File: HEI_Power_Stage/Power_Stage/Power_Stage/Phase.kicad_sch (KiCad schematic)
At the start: 41 parts, among them IC1 ACS730KLCTR-65ABT, IC5 AHV85111KNHTR, IC6 AHV85111KNHTR, Q1 EPC2304ENGRT, Q2 EPC2304ENGRT

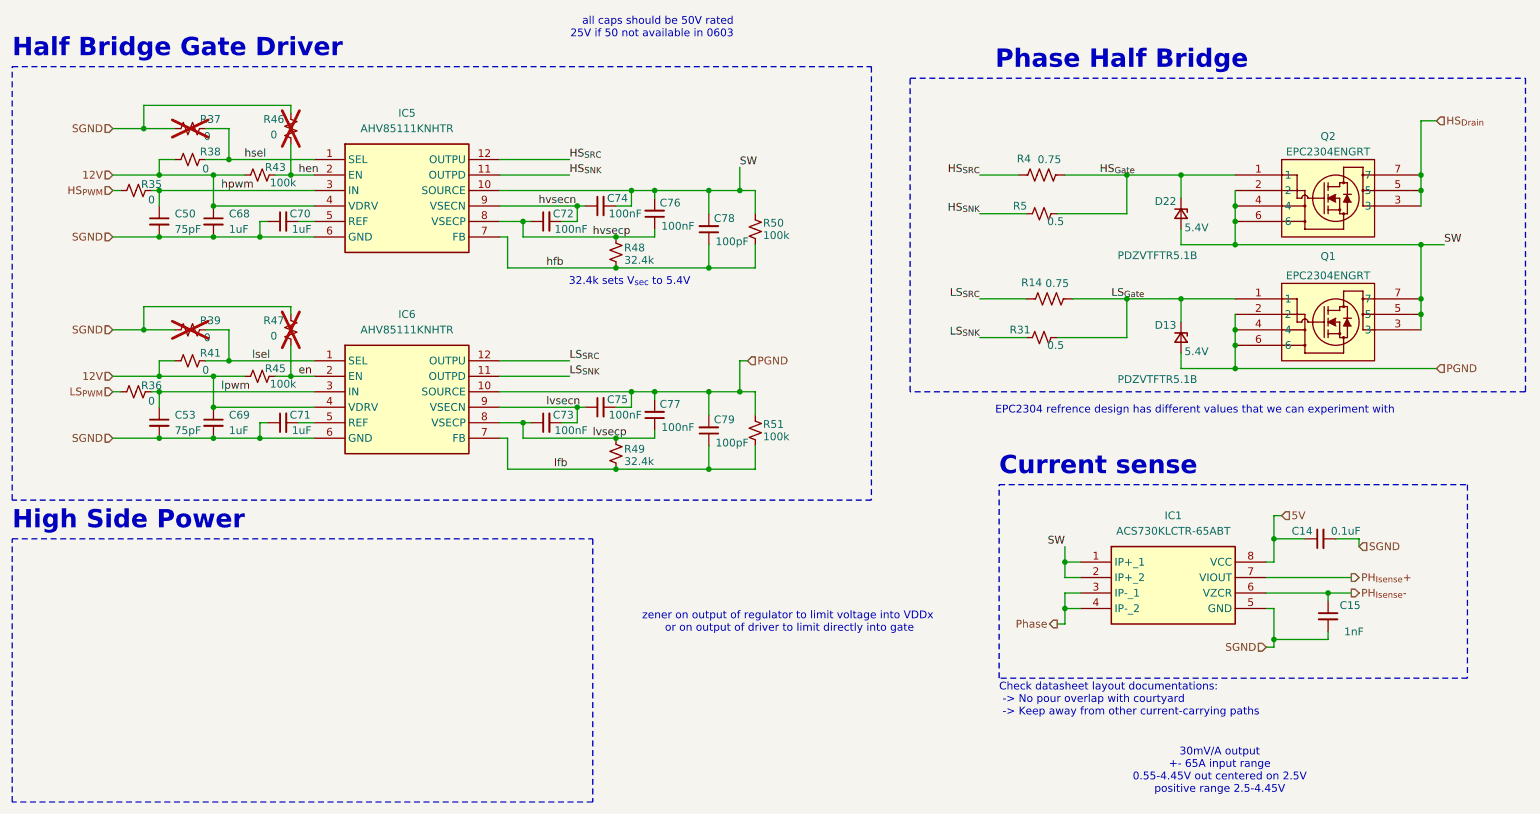
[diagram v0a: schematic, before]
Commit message: done
silkscreen done and bom done in digikey
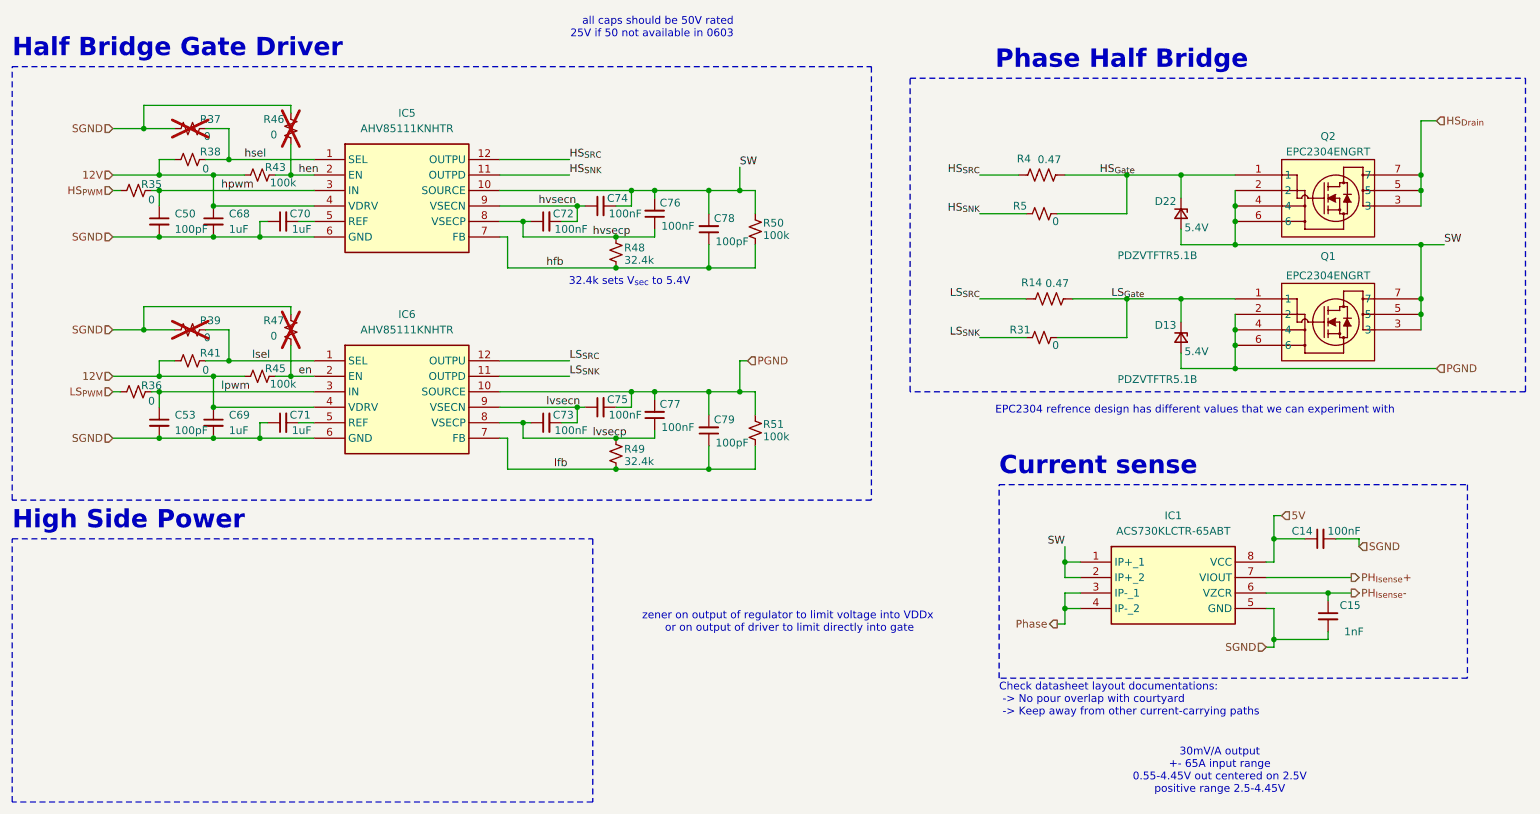
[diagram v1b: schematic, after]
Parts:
- C14: value 0.1uF -> 100nF
- C50, C53: value 75pF -> 100pF
- R14, R4: value 0.75 -> 0.47
- R31, R5: value 0.5 -> 0
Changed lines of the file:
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@@
 			)
 		)
-		(property "Value" "0.75"
+		(property "Value" "0.47"
 			(at 191.77 74.93 90)
 			(effects
@@
 			)
 		)
-		(property "Value" "0.1uF"
+		(property "Value" "100nF"
 			(at 241.554 115.57 90)
 			(effects
@@
 			)
 		)
-		(property "Value" "0.5"
+		(property "Value" "0"
 			(at 191.516 85.09 90)
 			(effects
@@
 			)
 		)
-		(property "Value" "0.75"
+		(property "Value" "0.47"
 			(at 190.5 54.61 90)
 			(effects
@@
 			)
 		)
-		(property "Value" "75pF"
+		(property "Value" "100pF"
 			(at 46.99 66.0462 0)
 			(effects
@@
 			)
 		)
-		(property "Value" "0.5"
+		(property "Value" "0"
 			(at 191.516 64.77 90)
 			(effects
@@
 			)
 		)
-		(property "Value" "75pF"
+		(property "Value" "100pF"
 			(at 46.99 99.0662 0)
 			(effects

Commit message: some changes
isolated amplifier now self powered so removed old amp and iso power supply
gate return paths now on layer two
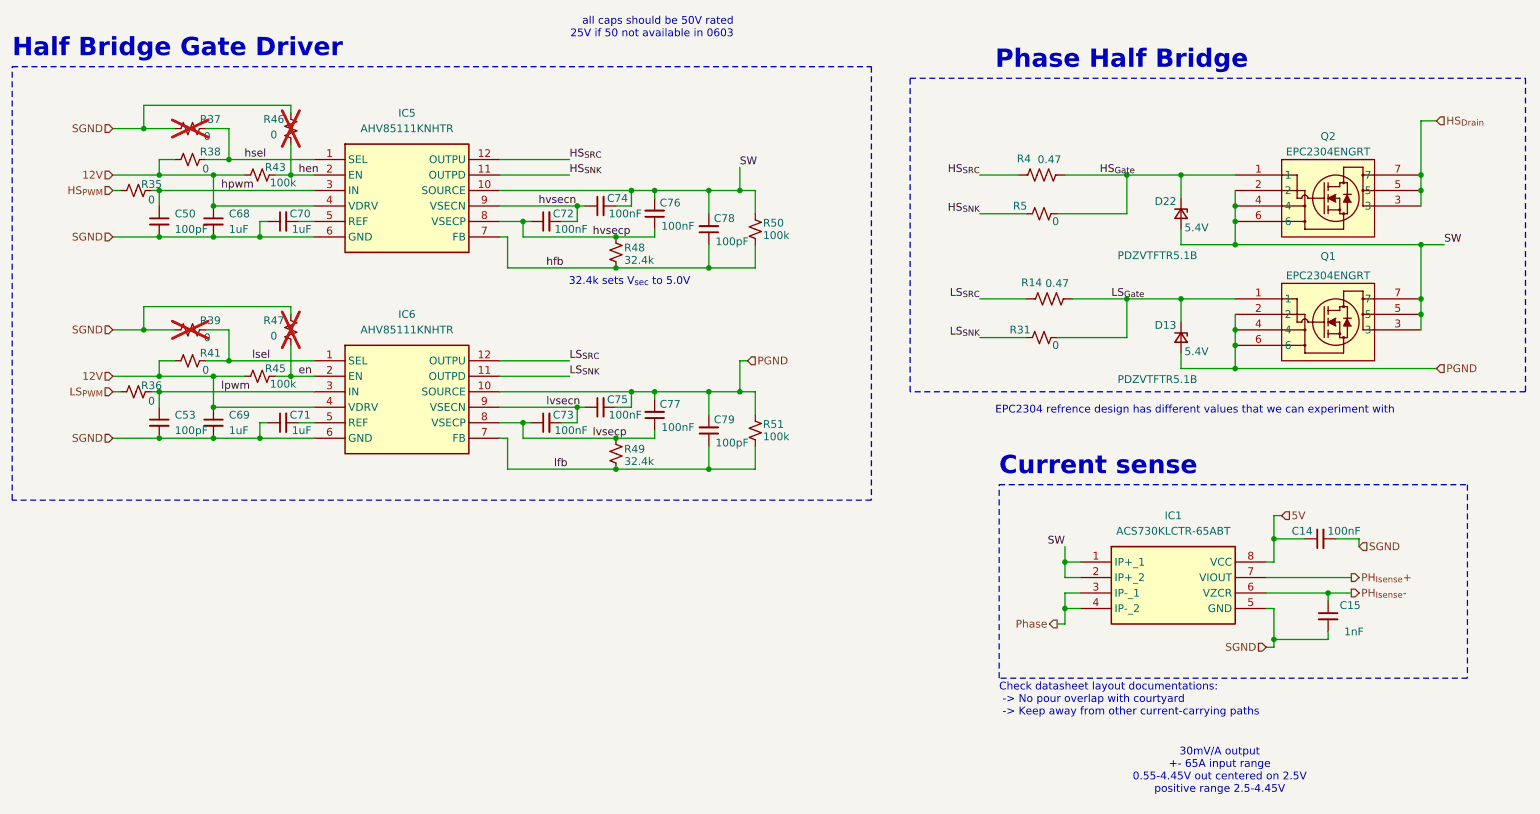
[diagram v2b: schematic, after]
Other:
- note added: "32.4k sets V_{sec} to 5.0V"
- note removed: "32.4k sets V_{sec} to 5.4V"
- note removed: "High Side Power"
- note removed: "zener on output of regulator to limit voltage into VDDx or on output of driver to limit directly into gate"
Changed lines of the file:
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@@
 		)
 	)
-	(rectangle
-		(start 20.32 116.84)
-		(end 115.57 160.02)
-		(stroke
-			(width 0)
-			(type dash)
-		)
-		(fill
-			(type none)
-		)
-	)
-	(text "32.4k sets V_{sec} to 5.4V"
+	(text "32.4k sets V_{sec} to 5.0V\n"
 		(exclude_from_sim no)
 		(at 131.572 74.676 0)
@@
 			)
 			(justify right)
-		)
-	)
-	(text "zener on output of regulator to limit voltage into VDDx\n or on output of driver to limit directly into gate"
-		(exclude_from_sim no)
-		(at 147.574 130.556 0)
-		(effects
-			(font
-				(size 1.27 1.27)
-			)
 		)
 	)
@@
 			)
 			(justify left bottom)
-		)
-	)
-	(text "High Side Power\n"
-		(exclude_from_sim no)
-		(at 20.32 115.57 0)
-		(effects
-			(font
-				(size 3 3)
-				(thickness 0.254)
-				(bold yes)
-			)
-			(justify left bottom)
